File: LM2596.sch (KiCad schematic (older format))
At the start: 7 parts

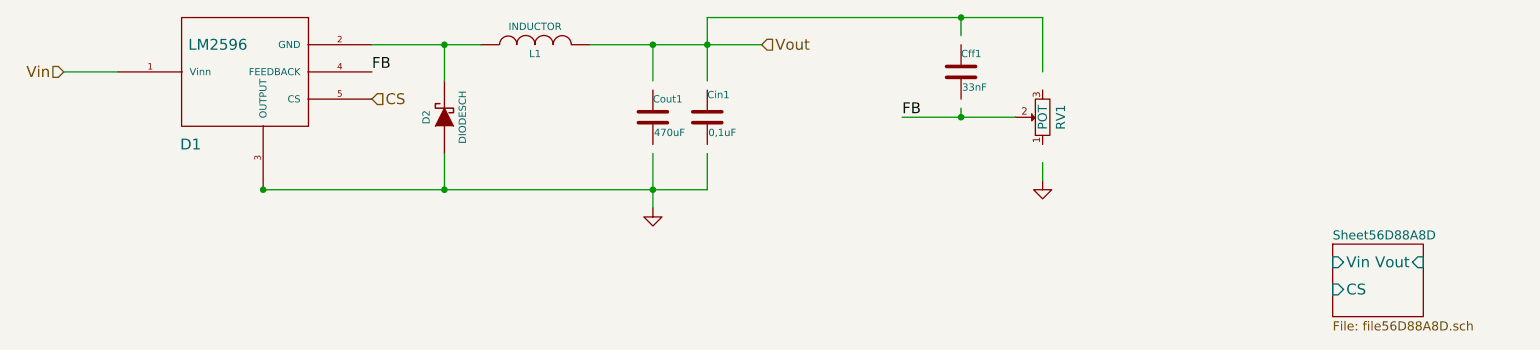
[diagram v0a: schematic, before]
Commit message: Подключены программатор, питание и генератор
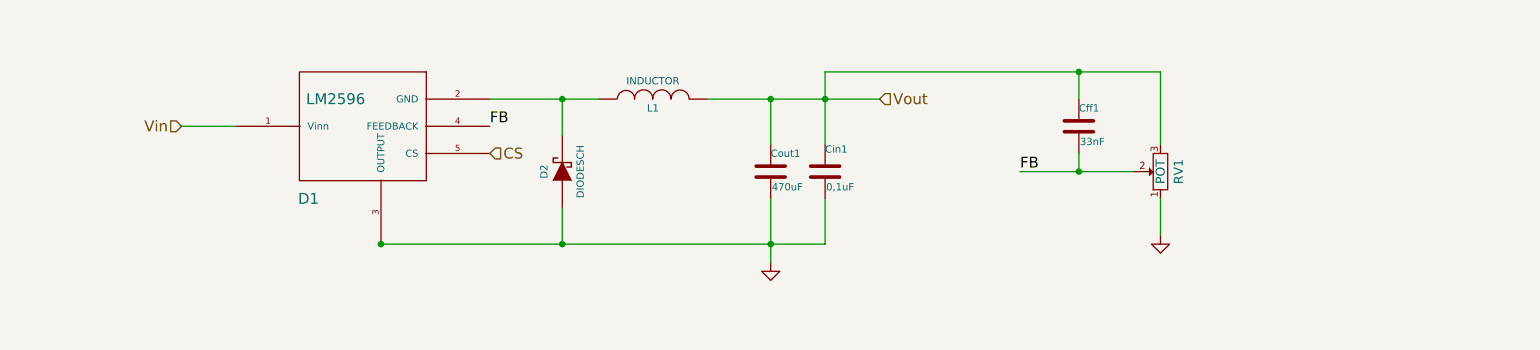
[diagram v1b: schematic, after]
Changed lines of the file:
@@
 EESchema Schematic File Version 2
-LIBS:lm2596
 LIBS:power
 LIBS:device
@@
 LIBS:memory
 LIBS:xilinx
-LIBS:special
 LIBS:microcontrollers
 LIBS:dsp
@@
 LIBS:contrib
 LIBS:valves
-LIBS:LM2596-cache
+LIBS:Pulse_Module-cache
 EELAYER 27 0
 EELAYER END
 $Descr A4 11693 8268
 encoding utf-8
-Sheet 1 2
+Sheet 2 3
 Title ""
-Date "4 mar 2016"
+Date "14 mar 2016"
 Rev ""
 Comp ""
@@
 $Comp
 L C Cin1
-U 1 1 56D4B859
-P 5700 3400
-F 0 "Cin1" H 5700 3500 40  0000 L BNN
-F 1 "0,1uF" H 5706 3315 40  0000 L CNN
-F 2 "~" V 5738 3250 30  0000 C CNN
-F 3 "~" H 5700 3400 60  0000 C CNN
-	1    5700 3400
+U 1 1 56DED62E
+P 6350 3700
+F 0 "Cin1" H 6350 3800 40  0000 L BNN
+F 1 "0,1uF" H 6356 3615 40  0000 L CNN
+F 2 "~" V 6388 3550 30  0000 C CNN
+F 3 "~" H 6350 3700 60  0000 C CNN
+	1    6350 3700
 	1    0    0    -1
 $EndComp
 $Comp
 L C Cff1
-U 1 1 56D4BBAC
-P 7100 3150
-F 0 "Cff1" H 7100 3250 40  0000 L CNN
-F 1 "33nF" H 7106 3065 40  0000 L CNN
-F 2 "~" H 7138 3000 30  0000 C CNN
-F 3 "~" H 7100 3150 60  0000 C CNN
-	1    7100 3150
+U 1 1 56DED634
+P 7750 3450
+F 0 "Cff1" H 7750 3550 40  0000 L CNN
+F 1 "33nF" H 7756 3365 40  0000 L CNN
+F 2 "~" H 7788 3300 30  0000 C CNN
+F 3 "~" H 7750 3450 60  0000 C CNN
+	1    7750 3450
 	1    0    0    -1
 $EndComp
 $Comp
 L DIODESCH D2
-U 1 1 56D4BC17
-P 4250 3400
-F 0 "D2" H 4250 3500 40  0000 C CNN
-F 1 "DIODESCH" H 4250 3300 40  0000 C CNN
-F 2 "~" H 4250 3400 60  0000 C CNN
-F 3 "~" H 4250 3400 60  0000 C CNN
-	1    4250 3400
+U 1 1 56DED63A
+P 4900 3700
+F 0 "D2" H 4900 3800 40  0000 C CNN
+F 1 "DIODESCH" H 4900 3600 40  0000 C CNN
+F 2 "~" H 4900 3700 60  0000 C CNN
+F 3 "~" H 4900 3700 60  0000 C CNN
+	1    4900 3700
 	0    -1   -1   0
 $EndComp
 $Comp
 L INDUCTOR L1
-U 1 1 56D4BC52
-P 4750 3000
-F 0 "L1" V 4700 3000 40  0000 C CNN
-F 1 "INDUCTOR" V 4850 3000 40  0000 C CNN
-F 2 "~" H 4750 3000 60  0000 C CNN
-F 3 "~" H 4750 3000 60  0000 C CNN
-	1    4750 3000
+U 1 1 56DED640
+P 5400 3300
+F 0 "L1" V 5350 3300 40  0000 C CNN
+F 1 "INDUCTOR" V 5500 3300 40  0000 C CNN
+F 2 "~" H 5400 3300 60  0000 C CNN
+F 3 "~" H 5400 3300 60  0000 C CNN
+	1    5400 3300
 	0    -1   -1   0
 $EndComp
 $Comp
 L C Cout1
-U 1 1 56D4BC6E
-P 5400 3400
-F 0 "Cout1" H 5400 3500 40  0000 L CNN
-F 1 "470uF" H 5406 3315 40  0000 L CNN
-F 2 "~" H 5438 3250 30  0000 C CNN
-F 3 "~" H 5400 3400 60  0000 C CNN
-	1    5400 3400
+U 1 1 56DED646
+P 6050 3700
+F 0 "Cout1" H 6050 3800 40  0000 L CNN
+F 1 "470uF" H 6056 3615 40  0000 L CNN
+F 2 "~" H 6088 3550 30  0000 C CNN
+F 3 "~" H 6050 3700 60  0000 C CNN
+	1    6050 3700
 	1    0    0    -1
 $EndComp
 Wire Wire Line
-	3850 3000 4450 3000
+	4500 3300 5100 3300
 Wire Wire Line
-	5050 3000 6000 3000
+	5700 3300 6650 3300
 Wire Wire Line
-	5400 3000 5400 3200
+	6050 3300 6050 3550
 Wire Wire Line
-	5700 2850 5700 3200
-Connection ~ 5400 3000
+	6350 3150 6350 3550
+Connection ~ 6050 3300
 Wire Wire Line
-	7100 2950 7100 2850
+	7750 3150 7750 3300
 Wire Wire Line
-	5700 2850 7550 2850
-Connection ~ 5700 3000
+	6350 3150 8200 3150
+Connection ~ 6350 3300
 Wire Wire Line
-	7550 2850 7550 3150
-Connection ~ 7100 2850
+	8200 3150 8200 3550
+Connection ~ 7750 3150
 Wire Wire Line
-	6775 3400 7400 3400
+	7425 3700 8050 3700
 Wire Wire Line
-	7100 3400 7100 3350
-Connection ~ 7100 3400
+	7750 3600 7750 3700
+Connection ~ 7750 3700
 Wire Wire Line
-	4250 3800 4250 3600
-Connection ~ 3250 3800
+	4900 4100 4900 3900
+Connection ~ 3900 4100
 Wire Wire Line
-	4250 3200 4250 3000
-Connection ~ 4250 3000
+	4900 3500 4900 3300
+Connection ~ 4900 3300
 Wire Wire Line
-	5400 3600 5400 3900
-Connection ~ 4250 3800
+	6050 3850 6050 4200
+Connection ~ 4900 4100
 Wire Wire Line
-	5700 3800 5700 3600
-Connection ~ 5400 3800
+	6350 3850 6350 4100
+Connection ~ 6050 4100
 Wire Wire Line
-	2150 3150 2450 3150
-Text HLabel 2150 3150 0    60   Input ~ 0
+	2800 3450 3100 3450
+Text HLabel 2800 3450 0    60   Input ~ 0
 Vin
-Text Label 3850 3150 0    60   ~ 0
+Text Label 4500 3450 0    60   ~ 0
 FB
-Text Label 6775 3400 0    60   ~ 0
+Text Label 7425 3700 0    60   ~ 0
 FB
-Text HLabel 6000 3000 2    60   Input ~ 0
+Text HLabel 6650 3300 2    60   Input ~ 0
 Vout
 $Comp
 L GND #PWR01
-U 1 1 56D87F66
-P 5400 3900
-F 0 "#PWR01" H 5400 3900 30  0001 C CNN
-F 1 "GND" H 5400 3830 30  0001 C CNN
-F 2 "" H 5400 3900 60  0000 C CNN
-F 3 "" H 5400 3900 60  0000 C CNN
-	1    5400 3900
+U 1 1 56DED666
+P 6050 4200
+F 0 "#PWR01" H 6050 4200 30  0001 C CNN
+F 1 "GND" H 6050 4130 30  0001 C CNN
+F 2 "" H 6050 4200 60  0000 C CNN
+F 3 "" H 6050 4200 60  0000 C CNN
+	1    6050 4200
 	1    0    0    -1
 $EndComp
 $Comp
 L GND #PWR02
-U 1 1 56D87F9C
-P 7550 3750
-F 0 "#PWR02" H 7550 3750 30  0001 C CNN
-F 1 "GND" H 7550 3680 30  0001 C CNN
-F 2 "" H 7550 3750 60  0000 C CNN
-F 3 "" H 7550 3750 60  0000 C CNN
-	1    7550 3750
+U 1 1 56DED66C
+P 8200 4050
+F 0 "#PWR02" H 8200 4050 30  0001 C CNN
+F 1 "GND" H 8200 3980 30  0001 C CNN
+F 2 "" H 8200 4050 60  0000 C CNN
+F 3 "" H 8200 4050 60  0000 C CNN
+	1    8200 4050
 	1    0    0    -1
 $EndComp
 Wire Wire Line
-	7550 3650 7550 3750
-Text HLabel 3850 3300 2    60   Input ~ 0
+	8200 3850 8200 4050
+Text HLabel 4500 3600 2    60   Input ~ 0
 CS
 $Comp
 L POT RV1
-U 1 1 56D881F7
-P 7550 3400
-F 0 "RV1" H 7550 3300 50  0000 C CNN
-F 1 "POT" H 7550 3400 50  0000 C CNN
-F 2 "~" H 7550 3400 60  0000 C CNN
-F 3 "~" H 7550 3400 60  0000 C CNN
-	1    7550 3400
+U 1 1 56DED674
+P 8200 3700
+F 0 "RV1" H 8200 3600 50  0000 C CNN
+F 1 "POT" H 8200 3700 50  0000 C CNN
+F 2 "~" H 8200 3700 60  0000 C CNN
+F 3 "~" H 8200 3700 60  0000 C CNN
+	1    8200 3700
 	0    -1   -1   0
 $EndComp
-$Sheet
-S 9150 4100 500  400
-U 56D88A8E
-F0 "Sheet56D88A8D" 50
-F1 "file56D88A8D.sch" 50
-F2 "Vin" I L 9150 4200 60
-F3 "Vout" I R 9650 4200 60
-F4 "CS" I L 9150 4350 60
-$EndSheet
 $Comp
 L LM2596 D1
-U 1 1 56D88146
-P 2800 2800
-F 0 "D1" H 2850 2050 60  0000 C CNN
-F 1 "LM2596" H 3000 2600 60  0000 C CNN
-F 2 "~" H 2800 2800 60  0000 C CNN
-F 3 "~" H 2800 2800 60  0000 C CNN
-	1    2800 2800
+U 1 1 56DED67A
+P 3450 3100
+F 0 "D1" H 3500 2350 60  0000 C CNN
+F 1 "LM2596" H 3650 2900 60  0000 C CNN
+F 2 "~" H 3450 3100 60  0000 C CNN
+F 3 "~" H 3450 3100 60  0000 C CNN
+	1    3450 3100
 	1    0    0    -1
 $EndComp
 Wire Wire Line
-	3250 3800 5700 3800
+	6350 4100 3900 4100
 $EndSCHEMATC

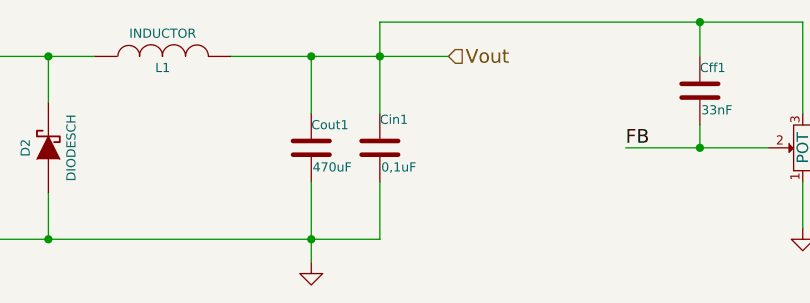
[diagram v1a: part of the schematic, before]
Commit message: Добавление 40пинового разъёма и UART
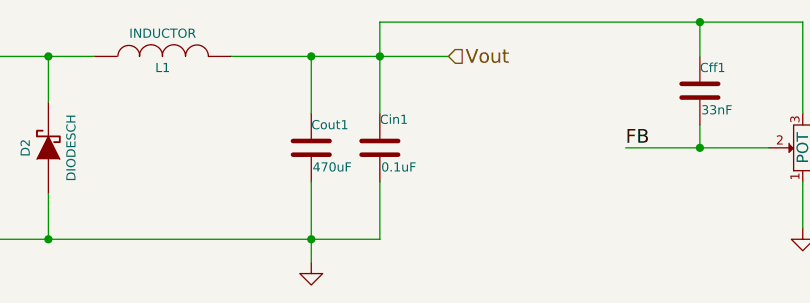
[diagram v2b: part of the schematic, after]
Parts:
- Cin1: value 0,1uF -> 0.1uF
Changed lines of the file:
@@
 EESchema Schematic File Version 2
+LIBS:pl2303
 LIBS:power
 LIBS:device
@@
 $Descr A4 11693 8268
 encoding utf-8
-Sheet 2 3
+Sheet 2 4
 Title ""
-Date "14 mar 2016"
+Date "7 apr 2016"
 Rev ""
 Comp ""
@@
 P 6350 3700
 F 0 "Cin1" H 6350 3800 40  0000 L BNN
-F 1 "0,1uF" H 6356 3615 40  0000 L CNN
+F 1 "0.1uF" H 6356 3615 40  0000 L CNN
 F 2 "~" V 6388 3550 30  0000 C CNN
 F 3 "~" H 6350 3700 60  0000 C CNN

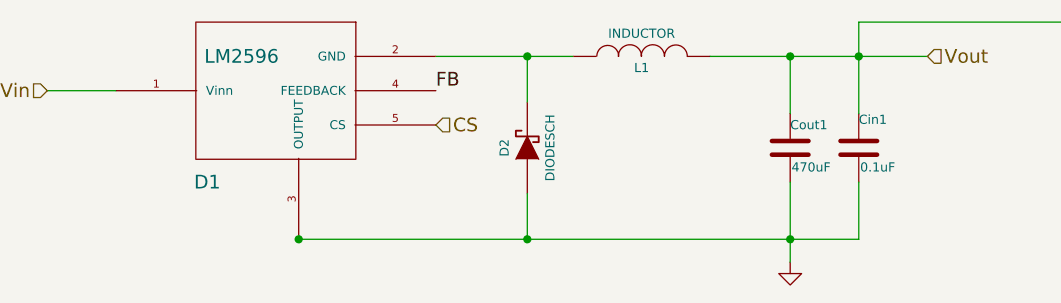
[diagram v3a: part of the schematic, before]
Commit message: Аннотированные элементы
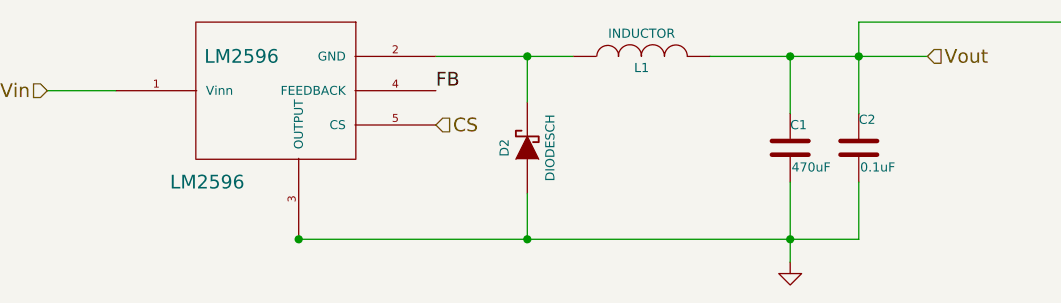
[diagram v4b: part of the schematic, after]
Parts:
- renumbered Cout1 to C1, Cin1 to C2, D1 to LM2596
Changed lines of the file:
@@
 Sheet 2 4
 Title ""
-Date "12 apr 2016"
+Date "13 apr 2016"
 Rev ""
 Comp ""
@@
 $EndDescr
 $Comp
-L C Cin1
+L C C2
 U 1 1 56DED62E
 P 6350 3700
-F 0 "Cin1" H 6350 3800 40  0000 L BNN
+F 0 "C2" H 6350 3800 40  0000 L BNN
 F 1 "0.1uF" H 6356 3615 40  0000 L CNN
 F 2 "~" V 6388 3550 30  0000 C CNN
@@
 $EndComp
 $Comp
-L C Cout1
+L C C1
 U 1 1 56DED646
 P 6050 3700
-F 0 "Cout1" H 6050 3800 40  0000 L CNN
+F 0 "C1" H 6050 3800 40  0000 L CNN
 F 1 "470uF" H 6056 3615 40  0000 L CNN
 F 2 "~" H 6088 3550 30  0000 C CNN
@@
 $EndComp
 $Comp
-L LM2596 D1
+L LM2596 LM2596
 U 1 1 56DED67A
 P 3450 3100
-F 0 "D1" H 3500 2350 60  0000 C CNN
+F 0 "LM2596" H 3500 2350 60  0000 C CNN
 F 1 "LM2596" H 3650 2900 60  0000 C CNN
 F 2 "~" H 3450 3100 60  0000 C CNN

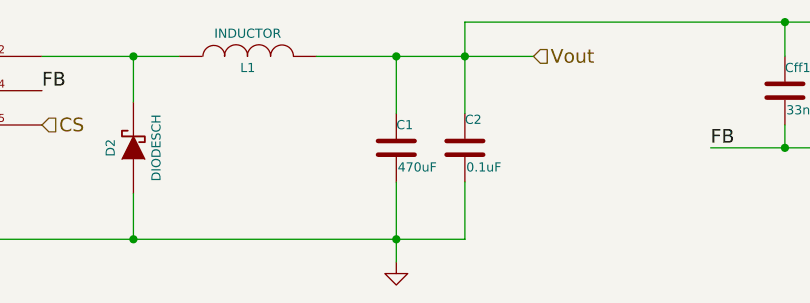
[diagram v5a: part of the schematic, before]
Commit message: Добавление WS2812, исправление всех замечаний
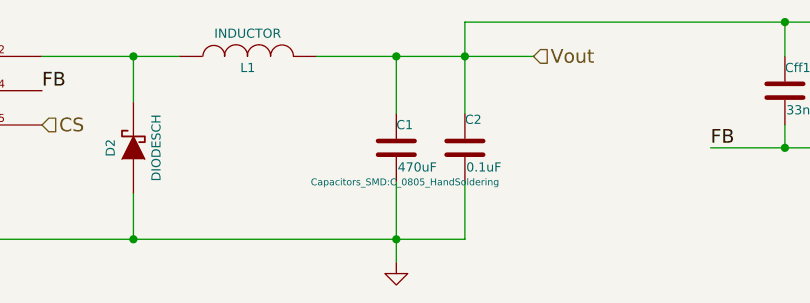
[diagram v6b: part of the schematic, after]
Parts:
- C1: footprint ~ -> Capacitors_SMD:C_0805_HandSoldering
- C2, Cff1, D2, L1, LM2596, RV1: footprint ~ -> (none)
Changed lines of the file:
@@
 EESchema Schematic File Version 2
+LIBS:Pulse_Module-rescue
 LIBS:conn3
 LIBS:pl2303
@@
 LIBS:philips
 LIBS:display
+LIBS:ws2812
 LIBS:cypress
 LIBS:siliconi
@@
 LIBS:valves
 LIBS:Pulse_Module-cache
-EELAYER 27 0
+EELAYER 25 0
 EELAYER END
 $Descr A4 11693 8268
@@
 F 0 "C2" H 6350 3800 40  0000 L BNN
 F 1 "0.1uF" H 6356 3615 40  0000 L CNN
-F 2 "~" V 6388 3550 30  0000 C CNN
+F 2 "" V 6388 3550 30  0001 C CNN
 F 3 "~" H 6350 3700 60  0000 C CNN
 	1    6350 3700
@@
 F 0 "Cff1" H 7750 3550 40  0000 L CNN
 F 1 "33nF" H 7756 3365 40  0000 L CNN
-F 2 "~" H 7788 3300 30  0000 C CNN
+F 2 "" H 7788 3300 30  0001 C CNN
 F 3 "~" H 7750 3450 60  0000 C CNN
 	1    7750 3450
@@
 F 0 "D2" H 4900 3800 40  0000 C CNN
 F 1 "DIODESCH" H 4900 3600 40  0000 C CNN
-F 2 "~" H 4900 3700 60  0000 C CNN
+F 2 "" H 4900 3700 60  0001 C CNN
 F 3 "~" H 4900 3700 60  0000 C CNN
 	1    4900 3700
@@
 F 0 "L1" V 5350 3300 40  0000 C CNN
 F 1 "INDUCTOR" V 5500 3300 40  0000 C CNN
-F 2 "~" H 5400 3300 60  0000 C CNN
+F 2 "" H 5400 3300 60  0001 C CNN
 F 3 "~" H 5400 3300 60  0000 C CNN
 	1    5400 3300
@@
 F 0 "C1" H 6050 3800 40  0000 L CNN
 F 1 "470uF" H 6056 3615 40  0000 L CNN
-F 2 "~" H 6088 3550 30  0000 C CNN
+F 2 "Capacitors_SMD:C_0805_HandSoldering" H 6088 3550 30  0000 C CNN
 F 3 "~" H 6050 3700 60  0000 C CNN
 	1    6050 3700
@@
 Vout
 $Comp
-L GND #PWR1
+L GND #PWR01
 U 1 1 56DED666
 P 6050 4200
-F 0 "#PWR1" H 6050 4200 30  0001 C CNN
+F 0 "#PWR01" H 6050 4200 30  0001 C CNN
 F 1 "GND" H 6050 4130 30  0001 C CNN
 F 2 "" H 6050 4200 60  0000 C CNN
@@
 $EndComp
 $Comp
-L GND #PWR2
+L GND #PWR02
 U 1 1 56DED66C
 P 8200 4050
-F 0 "#PWR2" H 8200 4050 30  0001 C CNN
+F 0 "#PWR02" H 8200 4050 30  0001 C CNN
 F 1 "GND" H 8200 3980 30  0001 C CNN
 F 2 "" H 8200 4050 60  0000 C CNN
@@
 F 0 "RV1" H 8200 3600 50  0000 C CNN
 F 1 "POT" H 8200 3700 50  0000 C CNN
-F 2 "~" H 8200 3700 60  0000 C CNN
+F 2 "" H 8200 3700 60  0001 C CNN
 F 3 "~" H 8200 3700 60  0000 C CNN
 	1    8200 3700
@@
 F 0 "LM2596" H 3500 2350 60  0000 C CNN
 F 1 "LM2596" H 3650 2900 60  0000 C CNN
-F 2 "~" H 3450 3100 60  0000 C CNN
+F 2 "" H 3450 3100 60  0001 C CNN
 F 3 "~" H 3450 3100 60  0000 C CNN
 	1    3450 3100

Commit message: Изменения в CvPCB
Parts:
- removed RV1: POT, symbol POT
- added R14, R15: R, Resistors_SMD:R_0402, symbol R
- C2: footprint (none) -> Capacitors_SMD:C_0402
- Cff1: footprint (none) -> Capacitors_SMD:C_0603_HandSoldering
- D2: footprint (none) -> Diodes_SMD:DO-214AB
- L1: footprint (none) -> Inductors:NR4018
- LM2596: footprint (none) -> TO_SOT_Packages_SMD:TO-263-5Lead
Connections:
- net FB: now also R14.2, R15.1
- net GND: now also R15.2
- net Vout: now also R14.1
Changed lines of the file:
@@
 F 0 "C2" H 6350 3800 40  0000 L BNN
 F 1 "0.1uF" H 6356 3615 40  0000 L CNN
-F 2 "" V 6388 3550 30  0001 C CNN
+F 2 "Capacitors_SMD:C_0402" V 6388 3550 30  0001 C CNN
 F 3 "~" H 6350 3700 60  0000 C CNN
 	1    6350 3700
@@
 F 0 "Cff1" H 7750 3550 40  0000 L CNN
 F 1 "33nF" H 7756 3365 40  0000 L CNN
-F 2 "" H 7788 3300 30  0001 C CNN
+F 2 "Capacitors_SMD:C_0603_HandSoldering" H 7788 3300 30  0001 C CNN
 F 3 "~" H 7750 3450 60  0000 C CNN
 	1    7750 3450
@@
 F 0 "D2" H 4900 3800 40  0000 C CNN
 F 1 "DIODESCH" H 4900 3600 40  0000 C CNN
-F 2 "" H 4900 3700 60  0001 C CNN
+F 2 "Diodes_SMD:DO-214AB" H 4900 3700 60  0001 C CNN
 F 3 "~" H 4900 3700 60  0000 C CNN
 	1    4900 3700
@@
 F 0 "L1" V 5350 3300 40  0000 C CNN
 F 1 "INDUCTOR" V 5500 3300 40  0000 C CNN
-F 2 "" H 5400 3300 60  0001 C CNN
+F 2 "Inductors:NR4018" H 5400 3300 60  0001 C CNN
 F 3 "~" H 5400 3300 60  0000 C CNN
 	1    5400 3300
@@
 	6350 3150 8200 3150
 Connection ~ 6350 3300
-Wire Wire Line
-	8200 3150 8200 3550
 Connection ~ 7750 3150
 Wire Wire Line
-	7425 3700 8050 3700
+	7425 3700 8200 3700
 Wire Wire Line
 	7750 3600 7750 3700
@@
 Connection ~ 4900 4100
 Wire Wire Line
-	6350 3850 6350 4100
+	6350 4100 6350 3850
 Connection ~ 6050 4100
 Wire Wire Line
@@
 L GND #PWR02
 U 1 1 56DED66C
-P 8200 4050
-F 0 "#PWR02" H 8200 4050 30  0001 C CNN
-F 1 "GND" H 8200 3980 30  0001 C CNN
-F 2 "" H 8200 4050 60  0000 C CNN
-F 3 "" H 8200 4050 60  0000 C CNN
-	1    8200 4050
+P 8200 4300
+F 0 "#PWR02" H 8200 4300 30  0001 C CNN
+F 1 "GND" H 8200 4230 30  0001 C CNN
+F 2 "" H 8200 4300 60  0000 C CNN
+F 3 "" H 8200 4300 60  0000 C CNN
+	1    8200 4300
 	1    0    0    -1
 $EndComp
 Wire Wire Line
-	8200 3850 8200 4050
+	8200 4100 8200 4300
 Text HLabel 4500 3600 2    60   Input ~ 0
 CS
-$Comp
-L POT RV1
-U 1 1 56DED674
-P 8200 3700
-F 0 "RV1" H 8200 3600 50  0000 C CNN
-F 1 "POT" H 8200 3700 50  0000 C CNN
-F 2 "" H 8200 3700 60  0001 C CNN
-F 3 "~" H 8200 3700 60  0000 C CNN
-	1    8200 3700
-	0    -1   -1   0
-$EndComp
 $Comp
 L LM2596 LM2596
@@
 F 0 "LM2596" H 3500 2350 60  0000 C CNN
 F 1 "LM2596" H 3650 2900 60  0000 C CNN
-F 2 "" H 3450 3100 60  0001 C CNN
+F 2 "TO_SOT_Packages_SMD:TO-263-5Lead" H 3450 3100 60  0001 C CNN
 F 3 "~" H 3450 3100 60  0000 C CNN
 	1    3450 3100
@@
 $EndComp
 Wire Wire Line
-	6350 4100 3900 4100
+	3900 4100 6350 4100
+$Comp
+L R R14
+U 1 1 572B2DAD
+P 8200 3450
+F 0 "R14" V 8280 3450 50  0000 C CNN
+F 1 "R" V 8200 3450 50  0000 C CNN
+F 2 "Resistors_SMD:R_0402" V 8130 3450 50  0001 C CNN
+F 3 "" H 8200 3450 50  0000 C CNN
+	1    8200 3450
+	1    0    0    -1
+$EndComp
+$Comp
+L R R15
+U 1 1 572B2E55
+P 8200 3950
+F 0 "R15" V 8280 3950 50  0000 C CNN
+F 1 "R" V 8200 3950 50  0000 C CNN
+F 2 "Resistors_SMD:R_0402" V 8130 3950 50  0001 C CNN
+F 3 "" H 8200 3950 50  0000 C CNN
+	1    8200 3950
+	1    0    0    -1
+$EndComp
+Wire Wire Line
+	8200 3150 8200 3300
+Wire Wire Line
+	8200 3600 8200 3800
+Connection ~ 8200 3700
 $EndSCHEMATC

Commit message: Небольшие изменения
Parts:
- R14, R15: value R -> 1k
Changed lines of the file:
@@
 P 8200 3450
 F 0 "R14" V 8280 3450 50  0000 C CNN
-F 1 "R" V 8200 3450 50  0000 C CNN
+F 1 "1k" V 8200 3450 50  0000 C CNN
 F 2 "Resistors_SMD:R_0402" V 8130 3450 50  0001 C CNN
 F 3 "" H 8200 3450 50  0000 C CNN
@@
 P 8200 3950
 F 0 "R15" V 8280 3950 50  0000 C CNN
-F 1 "R" V 8200 3950 50  0000 C CNN
+F 1 "1k" V 8200 3950 50  0000 C CNN
 F 2 "Resistors_SMD:R_0402" V 8130 3950 50  0001 C CNN
 F 3 "" H 8200 3950 50  0000 C CNN
